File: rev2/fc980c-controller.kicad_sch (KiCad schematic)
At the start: 35 parts, among them J1 SWD, J2 USB, J3 KEYBOARD, SW1 BOOT0, U1 XC6206P332MR, U2 STM32F401CBUx, U3 USBLC6-2SC6, U4 M24C64-RMN6TP, U5 PCA9306DC, Y1 8MHz Cl 20pF

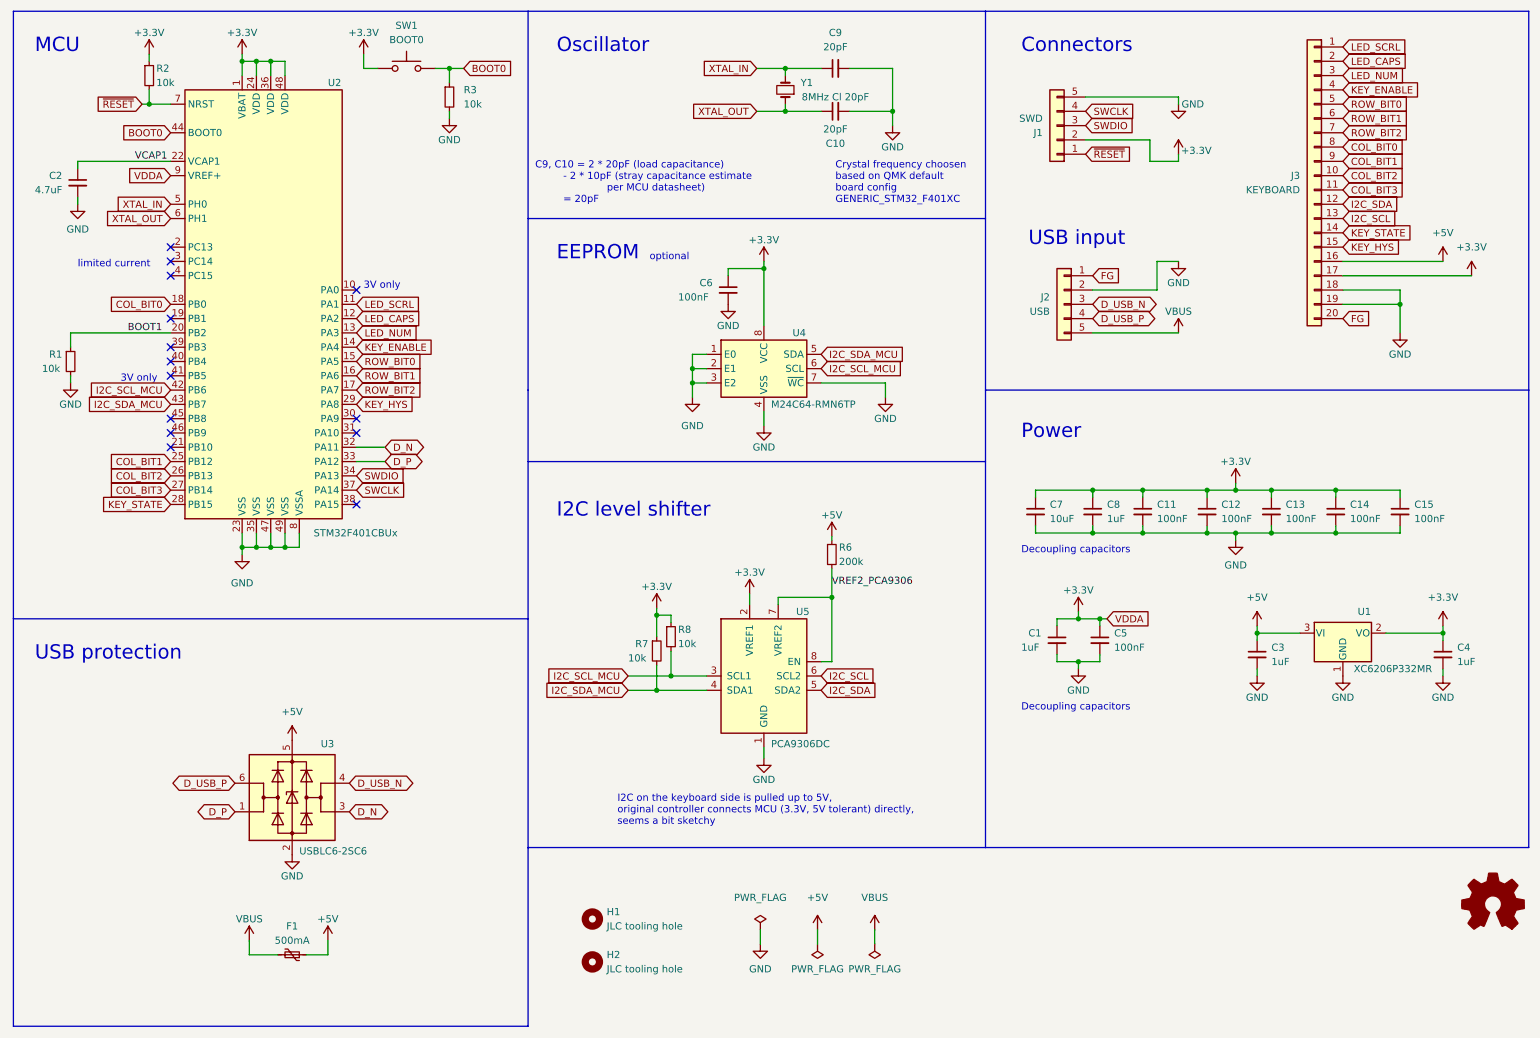
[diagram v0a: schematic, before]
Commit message: rev2: Add 5V pull-up to KEY_STATE pin
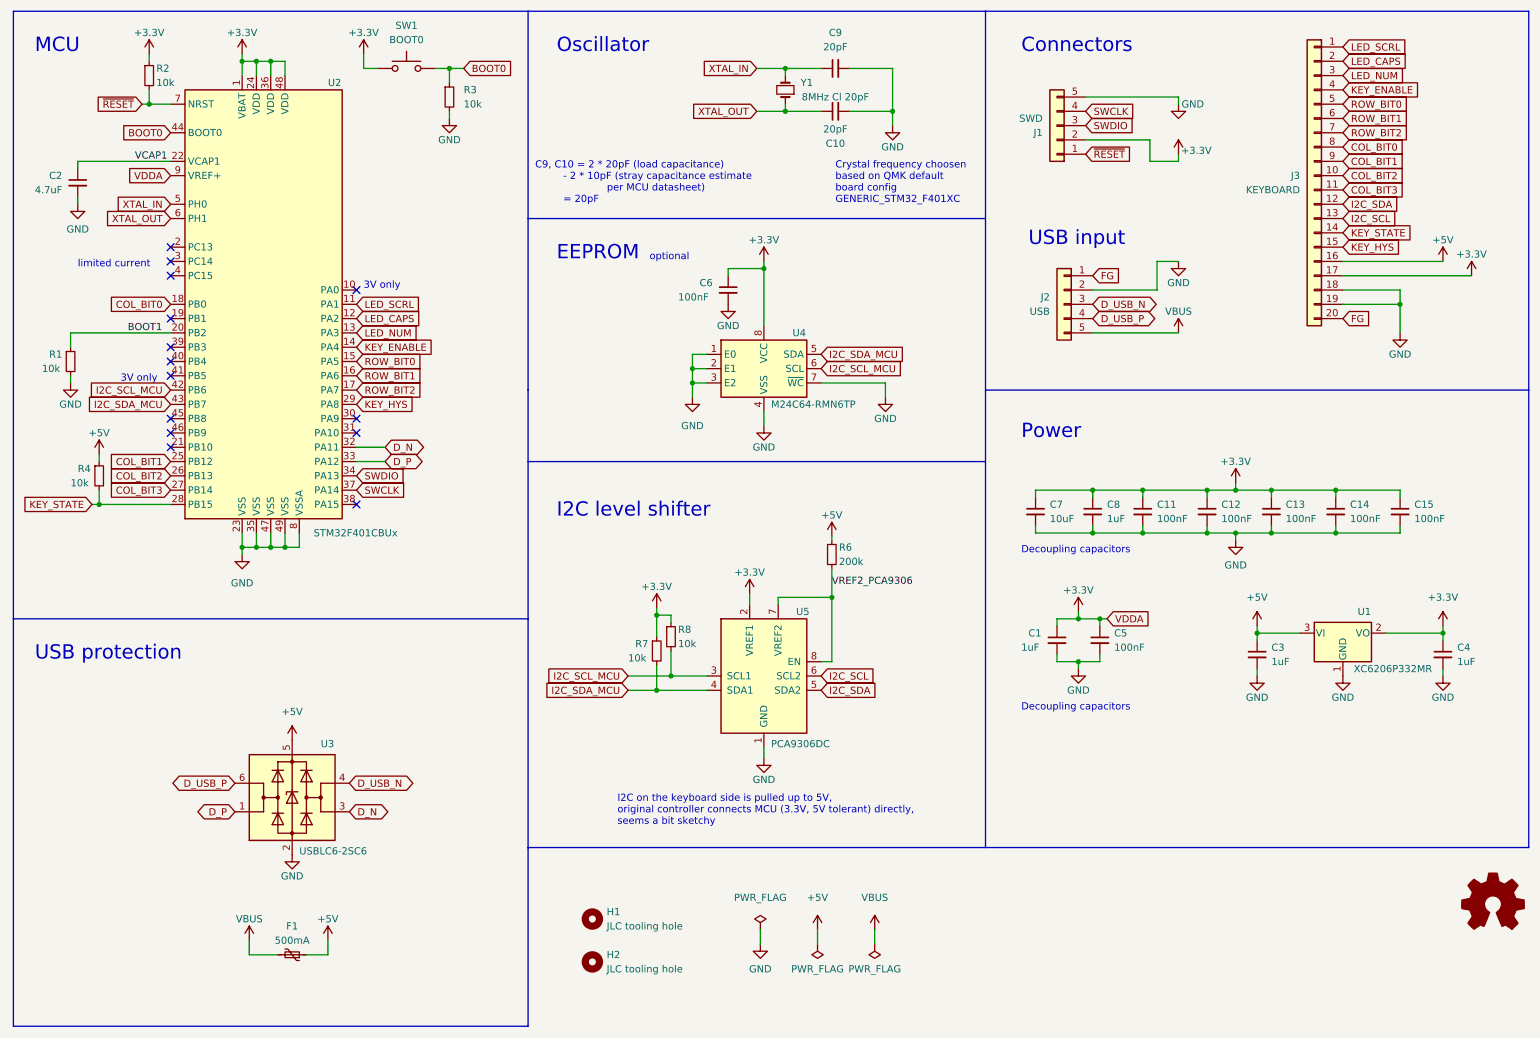
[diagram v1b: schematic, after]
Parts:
- added R4: 10k, Resistor_SMD:R_0402_1005Metric, symbol Device:R_Small
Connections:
- net +5V: now also R4.1
- net KEY_STATE: now also R4.2
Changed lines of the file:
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@@
   (junction (at 62.23 110.49) (diameter 0) (color 0 0 0 0)
+  )
+  (junction (at 29.21 102.87) (diameter 0) (color 0 0 0 0)
   )
   (junction (at 170.18 33.02) (diameter 0) (color 0 0 0 0)
@@
     (stroke (width 0) (type default) (color 0 0 0 0))
   )
+  (wire (pts (xy 27.94 102.87) (xy 29.21 102.87))
+    (stroke (width 0) (type default) (color 0 0 0 0))
+  )
   (polyline (pts (xy 105.41 95.25) (xy 186.69 95.25))
     (stroke (width 0) (type default) (color 0 0 0 0))
@@
     (stroke (width 0) (type default) (color 0 0 0 0))
   )
+  (wire (pts (xy 29.21 102.87) (xy 41.91 102.87))
+    (stroke (width 0) (type default) (color 0 0 0 0))
+  )
   (wire (pts (xy 134.62 81.28) (xy 137.16 81.28))
     (stroke (width 0) (type default) (color 0 0 0 0))
@@
     (stroke (width 0) (type default) (color 0 0 0 0))
   )
+  (wire (pts (xy 29.21 100.33) (xy 29.21 102.87))
+    (stroke (width 0) (type default) (color 0 0 0 0))
+  )
   (wire (pts (xy 57.15 110.49) (xy 59.69 110.49))
     (stroke (width 0) (type default) (color 0 0 0 0))
@@
   )
   (wire (pts (xy 25.4 41.91) (xy 25.4 43.18))
+    (stroke (width 0) (type default) (color 0 0 0 0))
+  )
+  (wire (pts (xy 29.21 93.98) (xy 29.21 95.25))
     (stroke (width 0) (type default) (color 0 0 0 0))
   )
@@
     )
   )
-  (global_label "KEY_STATE" (shape input) (at 41.91 102.87 180) (fields_autoplaced)
+  (global_label "KEY_STATE" (shape input) (at 27.94 102.87 180) (fields_autoplaced)
     (effects (font (size 1.27 1.27)) (justify right))
-    (property "Intersheet References" "${INTERSHEET_REFS}" (id 0) (at 29.6393 102.7906 0)
+    (property "Intersheet References" "${INTERSHEET_REFS}" (id 0) (at 15.6693 102.7906 0)
       (effects (font (size 1.27 1.27)) (justify right) hide)
     )
@@
     (pin "1")
   )
+  (symbol (lib_id "Device:R_Small") (at 29.21 97.79 0) (unit 1)
+    (in_bom yes) (on_board yes)
+    (property "Reference" "R4" (id 0) (at 25.4 96.52 0)
+      (effects (font (size 1.27 1.27)) (justify left))
+    )
+    (property "Value" "10k" (id 1) (at 24.13 99.06 0)
+      (effects (font (size 1.27 1.27)) (justify left))
+    )
+    (property "Footprint" "Resistor_SMD:R_0402_1005Metric" (id 2) (at 29.21 97.79 0)
+      (effects (font (size 1.27 1.27)) hide)
+    )
+    (property "Datasheet" "~" (id 3) (at 29.21 97.79 0)
+      (effects (font (size 1.27 1.27)) hide)
+    )
+    (pin "1")
+    (pin "2")
+  )
   (symbol (lib_id "power:+5V") (at 267.97 59.69 0) (mirror y) (unit 1)
-    (in_bom yes) (on_board yes) (fields_autoplaced)
+    (in_bom yes) (on_board yes)
     (property "Reference" "#PWR022" (id 0) (at 267.97 63.5 0)
       (effects (font (size 1.27 1.27)) hide)
     )
-    (property "Value" "+5V" (id 1) (at 267.97 54.61 0))
+    (property "Value" "+5V" (id 1) (at 267.97 55.88 0))
     (property "Footprint" "" (id 2) (at 267.97 59.69 0)
       (effects (font (size 1.27 1.27)) hide)
@@
   )
   (symbol (lib_id "power:+3.3V") (at 273.05 62.23 0) (mirror y) (unit 1)
-    (in_bom yes) (on_board yes) (fields_autoplaced)
+    (in_bom yes) (on_board yes)
     (property "Reference" "#PWR019" (id 0) (at 273.05 66.04 0)
       (effects (font (size 1.27 1.27)) hide)
     )
-    (property "Value" "+3.3V" (id 1) (at 273.05 57.15 0))
+    (property "Value" "+3.3V" (id 1) (at 273.05 58.42 0))
     (property "Footprint" "" (id 2) (at 273.05 62.23 0)
       (effects (font (size 1.27 1.27)) hide)
@@
     (pin "2")
     (pin "3")
+  )
+  (symbol (lib_name "+5V_1") (lib_id "power:+5V") (at 29.21 93.98 0) (unit 1)
+    (in_bom yes) (on_board yes)
+    (property "Reference" "#PWR010" (id 0) (at 29.21 97.79 0)
+      (effects (font (size 1.27 1.27)) hide)
+    )
+    (property "Value" "+5V" (id 1) (at 29.21 90.17 0))
+    (property "Footprint" "" (id 2) (at 29.21 93.98 0)
+      (effects (font (size 1.27 1.27)) hide)
+    )
+    (property "Datasheet" "" (id 3) (at 29.21 93.98 0)
+      (effects (font (size 1.27 1.27)) hide)
+    )
+    (pin "1")
   )
   (symbol (lib_id "Device:R_Small") (at 91.44 30.48 0) (unit 1)
@@
       (reference "#PWR09") (unit 1) (value "GND") (footprint "")
     )
+    (path "/9e5c5f4d-c4a7-480a-99a4-9bf3b3cc02e9"
+      (reference "#PWR010") (unit 1) (value "+5V") (footprint "")
+    )
     (path "/2dcefcfc-1d1d-4ee3-a677-60f96d75783a"
       (reference "#PWR011") (unit 1) (value "+5V") (footprint "")
@@
       (reference "R3") (unit 1) (value "10k") (footprint "Resistor_SMD:R_0402_1005Metric")
     )
+    (path "/71ce440f-fb30-48c0-bbde-618d379a714e"
+      (reference "R4") (unit 1) (value "10k") (footprint "Resistor_SMD:R_0402_1005Metric")
+    )
     (path "/ae06dd18-ec1d-4497-962f-d84c49a81f80"

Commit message: rev2: Drop I2C level shifter
Upon further review, using a 5V I2C bus should be unproblematic with a
5V tolerant MCU due to the open-drain design.
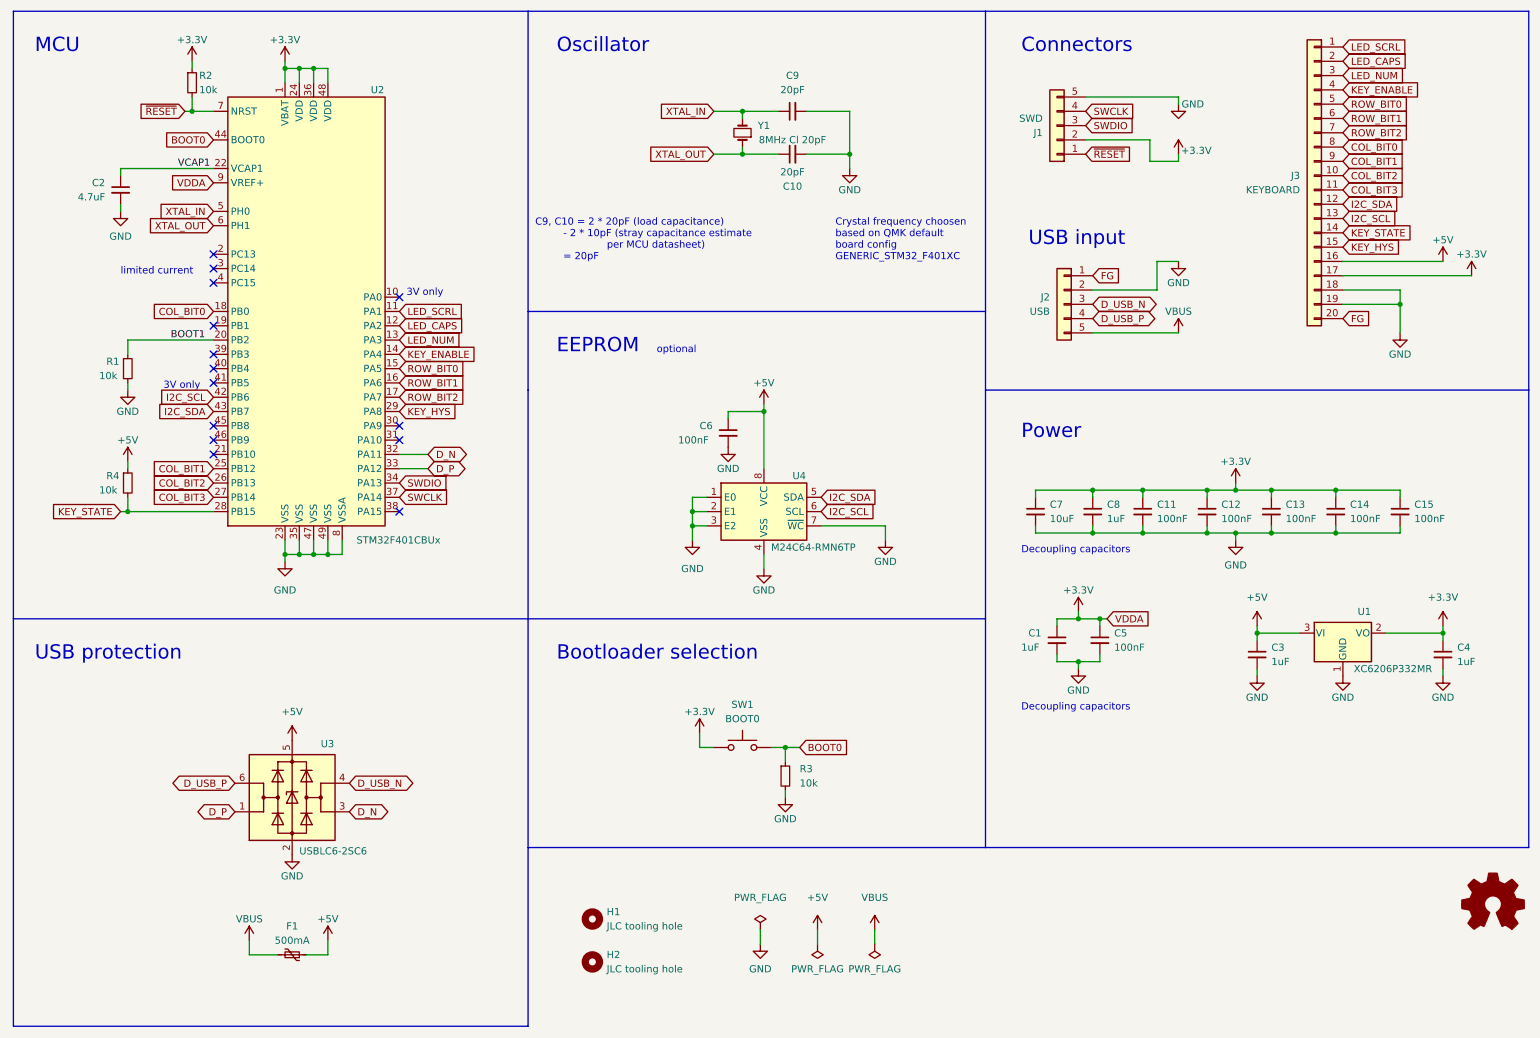
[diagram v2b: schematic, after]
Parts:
- removed R6: 200k, Resistor_SMD:R_0402_1005Metric, symbol Device:R_Small
- removed R7, R8: 10k, Resistor_SMD:R_0402_1005Metric, symbol Device:R_Small
- removed U5: PCA9306DC, Package_SO:VSSOP-8_2.3x2mm_P0.5mm, symbol Interface:PCA9306DC
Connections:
- net I2C_SCL_MCU is gone; now on net I2C_SCL: U2.42 (PB6), U4.6 (SCL)
- net I2C_SDA_MCU is gone; now on net I2C_SDA: U2.43 (PB7), U4.5 (SDA)
- net +3.3V: no longer C6.1, U4.8 (VCC)
- net +5V: now also C6.1, U4.8 (VCC)
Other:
- note added: "Bootloader selection"
- note removed: "I2C level shifter"
- note removed: "I2C on the keyboard side is pulled up to 5V, original controller connects MCU (3.3V, 5V tolerant) directly, seems a bit sketchy"
- moved on the sheet: C10, C2, C6, C9, R1, R2, R3, R4, SW1, U2, U4, Y1

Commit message: rev2: Fix typo in schematic
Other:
- note added: "Crystal frequency chosen based on QMK default board config GENERIC_STM32_F401XC"
- note removed: "Crystal frequency choosen based on QMK default board config GENERIC_STM32_F401XC"
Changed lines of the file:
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@@
     (effects (font (size 2.54 2.54)) (justify left bottom))
   )
-  (text "Crystal frequency choosen\nbased on QMK default\nboard config\nGENERIC_STM32_F401XC"
+  (text "Crystal frequency chosen\nbased on QMK default\nboard config\nGENERIC_STM32_F401XC"
     (at 160.02 59.69 0)
     (effects (font (size 1.27 1.27)) (justify left bottom))
